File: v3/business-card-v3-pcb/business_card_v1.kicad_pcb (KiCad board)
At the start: 16 copper layers, 89 x 51 mm, 70 parts, among them J1 Conn_01x05_Male, J2 Conn_01x01_Male, SW1 SW_SPST, U1 MIC5504-3.3YM5, U2 STM32G030F6P6

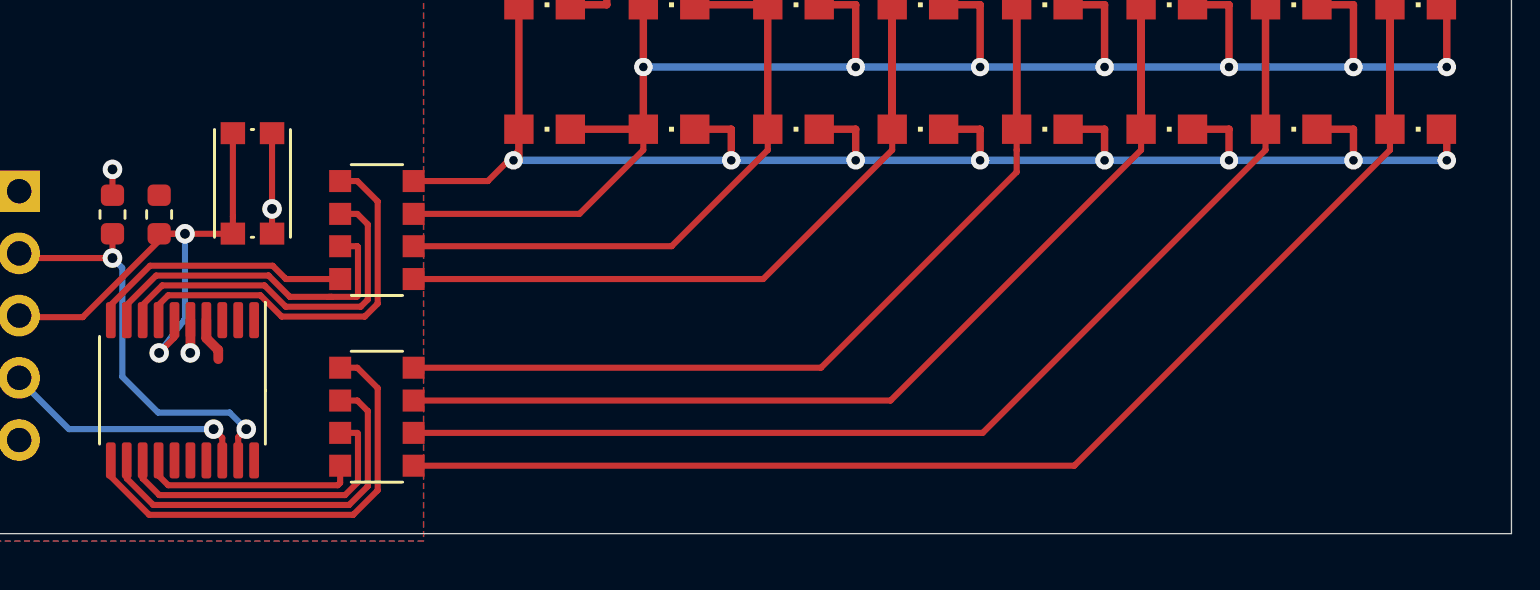
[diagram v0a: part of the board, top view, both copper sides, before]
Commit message: update to use a smaller resistor array
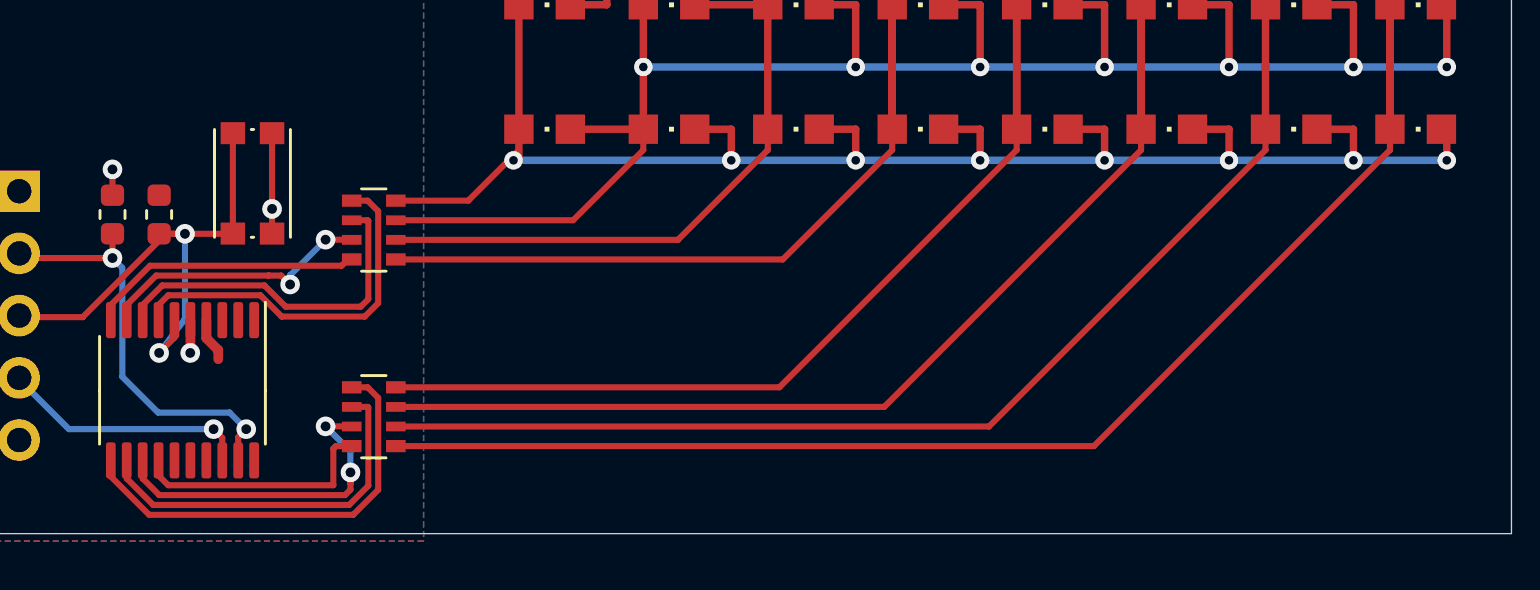
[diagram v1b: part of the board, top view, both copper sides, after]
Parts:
- RN1, RN2: footprint Resistor_SMD:R_Array_Convex_4x1206 -> Resistor_SMD:R_Array_Convex_4x0603
- moved RN1 0.13 mm to (146.6, 118.1)
- moved RN2 0.13 mm to (146.6, 125.7)
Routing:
- net PINC: track 13.8 -> 11.5 mm, vias 0 -> 2
- net PINH: track 8.94 -> 10.2 mm
- net PING: track 12.8 -> 13.8 mm, vias 0 -> 2
- net Net-(LED1-PadA): track 103.8 -> 104.9 mm
- net PINA: track 16.4 -> 15.3 mm
- net PINE: track 18.7 -> 17.7 mm
- net Net-(LED14-PadA): track 135.6 -> 136.4 mm
- net Net-(LED10-PadA): track 105.6 -> 106.4 mm
- net Net-(LED11-PadA): track 122.8 -> 123.5 mm
- net Net-(LED10-PadC): track 136.1 -> 136.8 mm
- net Net-(LED13-PadA): track 135.6 -> 136.1 mm
